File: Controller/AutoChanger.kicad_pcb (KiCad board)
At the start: 2 copper layers, 118 x 32 mm, 44 parts, among them IC1 ATMEGA328P, P1 CONNECT, P2 USB_B, P3 1, P4 2, P5 3, P6 4, P7 ICSP, SW1 RESET, SW2 1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

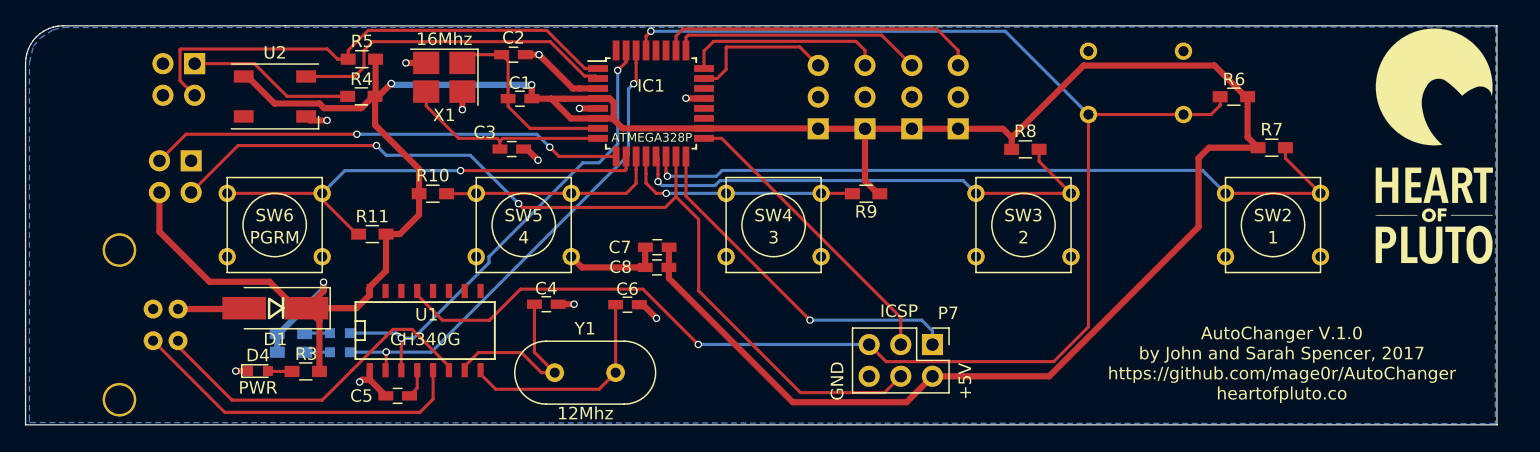
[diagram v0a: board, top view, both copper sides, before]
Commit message: Added a buzzer and moved pins.
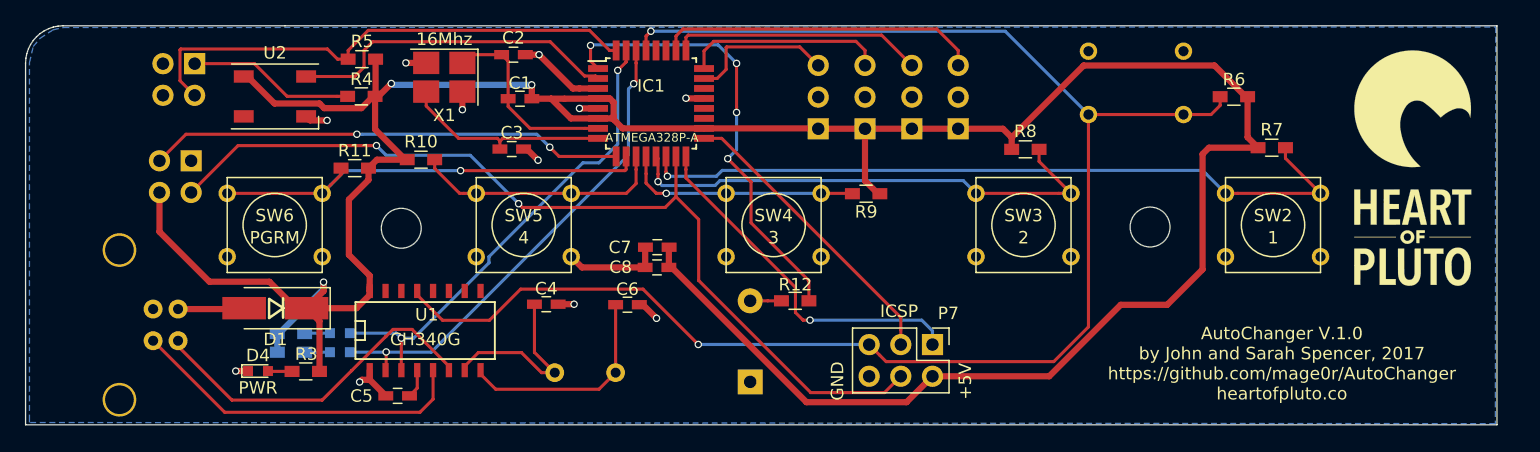
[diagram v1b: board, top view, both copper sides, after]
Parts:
- added R12: 100, Resistors_SMD:R_0603_HandSoldering, F.Cu at (150.9, 102.1)
- added REF**: M3, Mounting_Holes:MountingHole_3.2mm_M3, F.Cu at (119.3, 96.3)
- added REF**: M3, Mounting_Holes:MountingHole_3.2mm_M3, F.Cu at (179.4, 96.2)
- added SP1: SPEAKER, libs:piezo, B.Cu at (147.3, 105.4)
- IC1: value ATMEGA328P -> ATMEGA328P-A
- U3: value ITR9606 -> ITR9606-F
- Y1: moved to B.Cu
- moved R11 5.47 mm to (115.6, 91.5)
- moved R10 2.89 mm to (120.9, 90.8)
- moved G*** 2.46 mm to (200.4, 91.5)
- moved G*** 2.44 mm to (200.4, 91.5)
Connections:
- R5 pad 2: /D3 -> /D2
- U3 pad 3: /D3 -> /D2
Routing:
- net /D2: track 0.00 -> 41.5 mm
- net /D3: track 40.7 -> 36.5 mm, vias 0 -> 4
- net +5V: track 232.7 -> 236.1 mm
- net Net-(R12-Pad2): track 0.00 -> 2.51 mm
- net /D7: track 17.7 -> 20.2 mm
- net /D6: track 38.4 -> 37.0 mm
